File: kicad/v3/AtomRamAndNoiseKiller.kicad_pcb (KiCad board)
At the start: 2 copper layers, 76.2 x 49.5 mm, 26 parts, among them J1 Conn_01x10, J2 Conn_01x10, J3 Conn_01x03, J4 Conn_01x09, J5 Conn_01x09, J6 Conn_01x03, U1 74HCT14, U2 74HCT08, U3 74HCT245, U4 74HCT573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

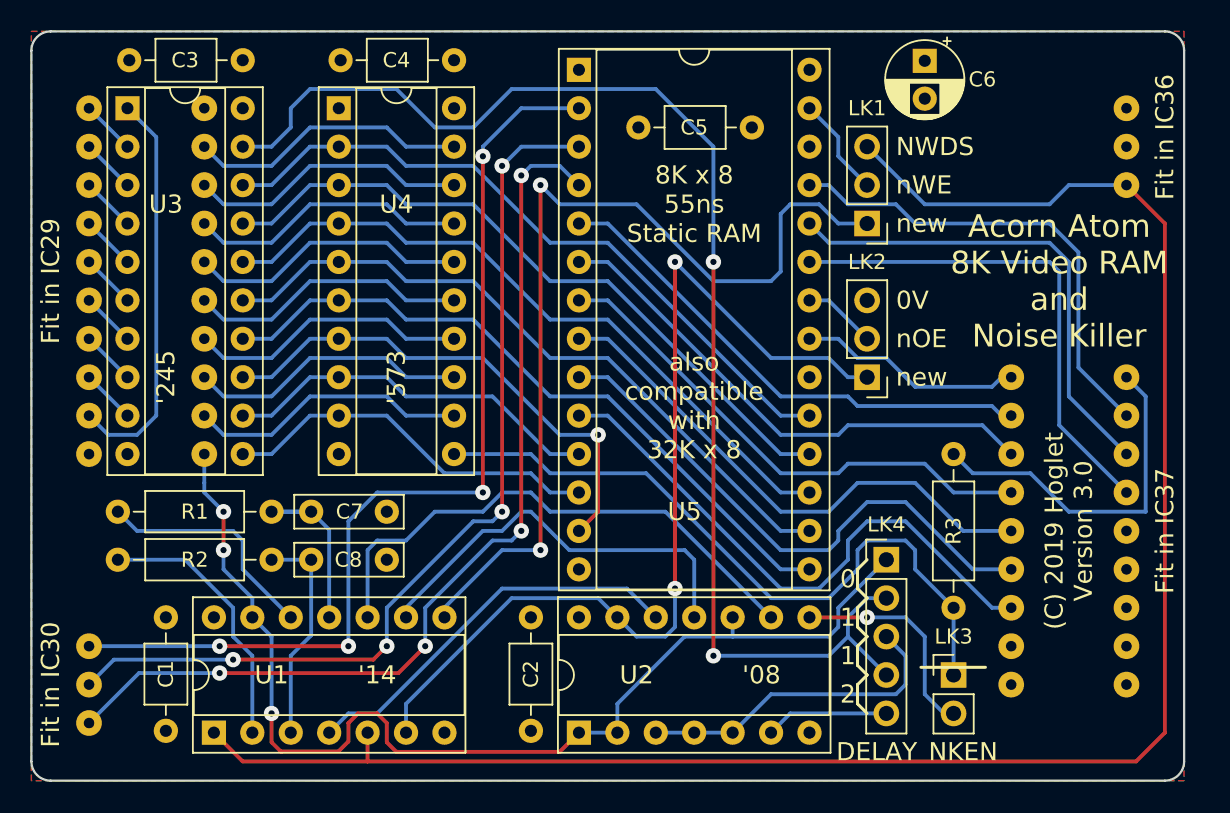
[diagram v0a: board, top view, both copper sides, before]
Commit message: Swapped NRDS and VDG on header
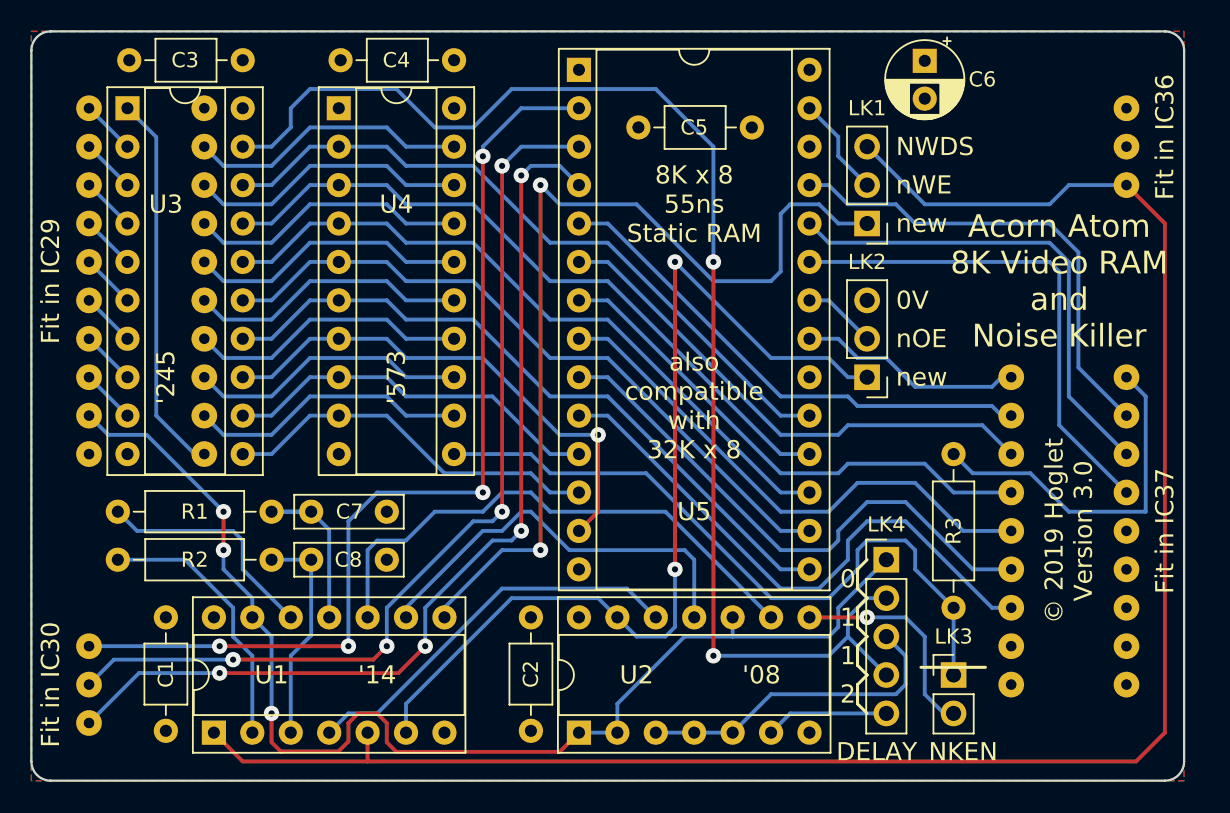
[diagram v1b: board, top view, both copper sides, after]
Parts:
- R1, R2: value 220R -> 270R
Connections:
- J1 pad 10: /NVDG -> /NDRS
- J2 pad 9: /NDRS -> /NVDG
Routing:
- net /NVDG: track 73.7 -> 80.9 mm
- net /NDRS: track 26.6 -> 25.3 mm
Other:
- board text added: "© 2019 Hoglet Version 3.0"
- board text removed: "(C) 2019 Hoglet Version 3.0"
